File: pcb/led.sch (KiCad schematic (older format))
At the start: 15 parts, among them J1 CONN_01X04, J2 CONN_01X04, J3 CONN_01X01, J4 CONN_01X01, J5 CONN_01X01, J6 CONN_01X01, U1 DSN-MINI-360, U2 MAX485, U3 MAX485

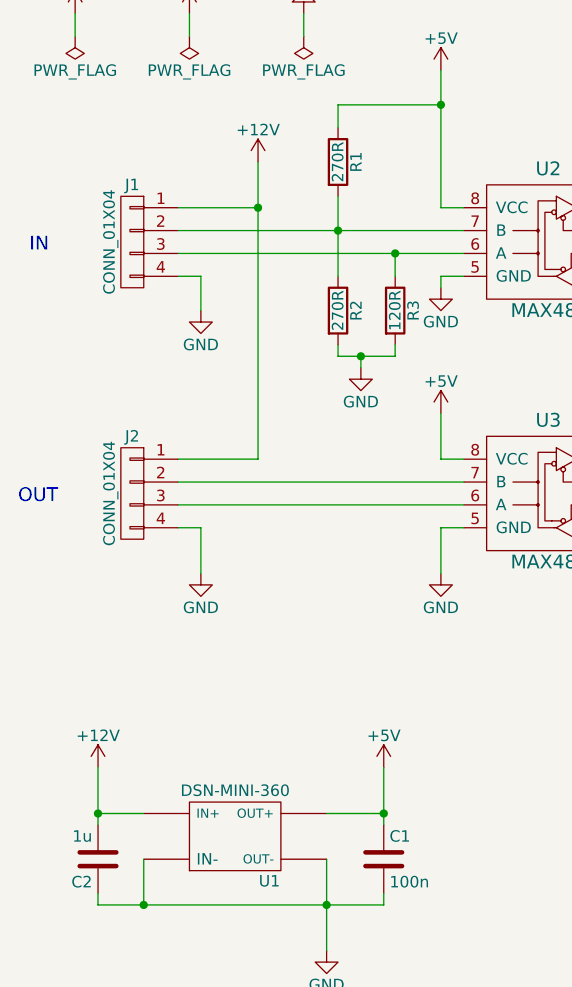
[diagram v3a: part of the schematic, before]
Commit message: Change to 3.5 mm pitch connectors. Finalize PCB layout.
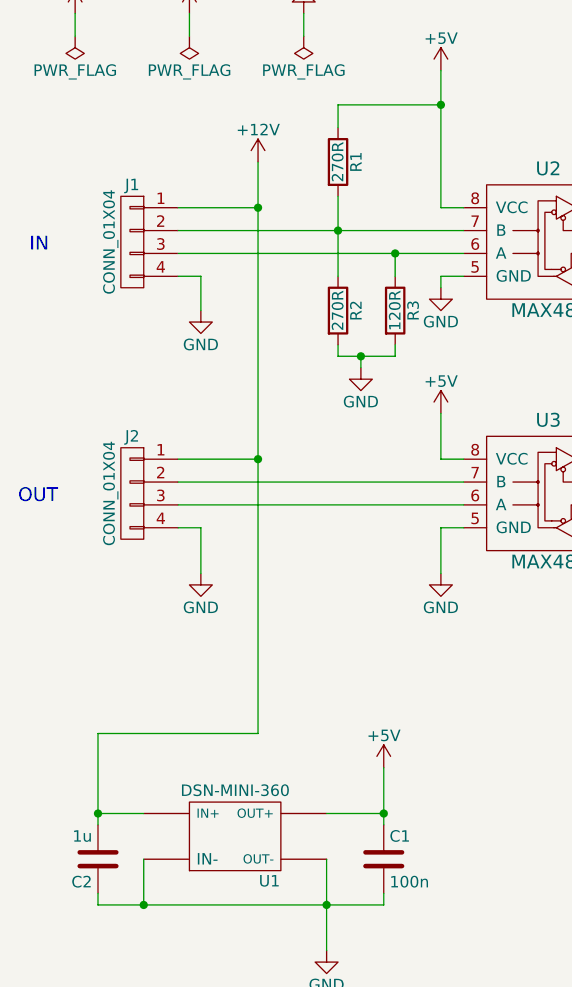
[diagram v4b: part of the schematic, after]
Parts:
- J1, J2: footprint Connectors_Phoenix:PhoenixContact_MSTBA-G_04x5.08mm_Angled -> Connectors_Phoenix:PhoenixContact_MC-G_04x3.50mm_Angled
- J3, J4, J5, J6: footprint Wire_Pads:SolderWirePad_single_1-5mmDrill -> Wire_Pads:SolderWirePad_single_1-2mmDrill
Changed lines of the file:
@@
 $EndDescr
 $Comp
-L +12V #PWR01
+L +12V #PWR5
 U 1 1 58CEE432
 P 1800 1550
-F 0 "#PWR01" H 1800 1400 50  0001 C CNN
+F 0 "#PWR5" H 1800 1400 50  0001 C CNN
 F 1 "+12V" H 1800 1690 50  0000 C CNN
 F 2 "" H 1800 1550 50  0001 C CNN
@@
 $EndComp
 $Comp
-L +12V #PWR02
+L +12V #PWR1
 U 1 1 58CEF552
 P 1000 900
-F 0 "#PWR02" H 1000 750 50  0001 C CNN
+F 0 "#PWR1" H 1000 750 50  0001 C CNN
 F 1 "+12V" H 1000 1040 50  0000 C CNN
 F 2 "" H 1000 900 50  0001 C CNN
@@
 Text Notes 800  1950 0    60   ~ 0
 IN
-Text Notes 5500 1900 0    60   ~ 0
-+5V
-Text Notes 5500 2150 0    60   ~ 0
-DI
-Text Notes 5500 2400 0    60   ~ 0
-DO
-Text Notes 5500 2650 0    60   ~ 0
-GND
 $Comp
 L C C2
@@
 $EndComp
 $Comp
-L PWR_FLAG #FLG03
+L PWR_FLAG #FLG1
 U 1 1 58CF1109
 P 1000 1000
-F 0 "#FLG03" H 1000 1075 50  0001 C CNN
+F 0 "#FLG1" H 1000 1075 50  0001 C CNN
 F 1 "PWR_FLAG" H 1000 1150 50  0000 C CNN
 F 2 "" H 1000 1000 50  0001 C CNN
@@
 $EndComp
 $Comp
-L +5V #PWR04
+L +5V #PWR16
 U 1 1 58CEF58A
 P 4950 1750
-F 0 "#PWR04" H 4950 1600 50  0001 C CNN
+F 0 "#PWR16" H 4950 1600 50  0001 C CNN
 F 1 "+5V" H 4950 1890 50  0000 C CNN
 F 2 "" H 4950 1750 50  0001 C CNN
@@
 $EndComp
 $Comp
-L GND #PWR05
+L GND #PWR17
 U 1 1 58CEF3EE
 P 4950 2700
-F 0 "#PWR05" H 4950 2450 50  0001 C CNN
+F 0 "#PWR17" H 4950 2450 50  0001 C CNN
 F 1 "GND" H 4950 2550 50  0000 C CNN
 F 2 "" H 4950 2700 50  0001 C CNN
@@
 F 0 "J1" H 1250 2150 50  0000 C CNN
 F 1 "CONN_01X04" V 1350 1900 50  0000 C CNN
-F 2 "Connectors_Phoenix:PhoenixContact_MSTBA-G_04x5.08mm_Angled" H 1250 1900 50  0001 C CNN
+F 2 "Connectors_Phoenix:PhoenixContact_MC-G_04x3.50mm_Angled" H 1250 1900 50  0001 C CNN
 F 3 "" H 1250 1900 50  0001 C CNN
 	1    1250 1900
@@
 F 0 "J2" H 1250 3250 50  0000 C CNN
 F 1 "CONN_01X04" V 1350 3000 50  0000 C CNN
-F 2 "Connectors_Phoenix:PhoenixContact_MSTBA-G_04x5.08mm_Angled" H 1250 3000 50  0001 C CNN
+F 2 "Connectors_Phoenix:PhoenixContact_MC-G_04x3.50mm_Angled" H 1250 3000 50  0001 C CNN
 F 3 "" H 1250 3000 50  0001 C CNN
 	1    1250 3000
@@
 $EndComp
 $Comp
-L GND #PWR06
+L GND #PWR3
 U 1 1 58D6FA50
 P 1550 2200
-F 0 "#PWR06" H 1550 1950 50  0001 C CNN
+F 0 "#PWR3" H 1550 1950 50  0001 C CNN
 F 1 "GND" H 1550 2050 50  0000 C CNN
 F 2 "" H 1550 2200 50  0001 C CNN
@@
 $EndComp
 $Comp
-L GND #PWR07
+L GND #PWR4
 U 1 1 58D6FA70
 P 1550 3350
-F 0 "#PWR07" H 1550 3100 50  0001 C CNN
+F 0 "#PWR4" H 1550 3100 50  0001 C CNN
 F 1 "GND" H 1550 3200 50  0000 C CNN
 F 2 "" H 1550 3350 50  0001 C CNN
@@
 OUT
 $Comp
-L GND #PWR08
+L GND #PWR7
 U 1 1 58D6FB2D
 P 2100 5000
-F 0 "#PWR08" H 2100 4750 50  0001 C CNN
+F 0 "#PWR7" H 2100 4750 50  0001 C CNN
 F 1 "GND" H 2100 4850 50  0000 C CNN
 F 2 "" H 2100 5000 50  0001 C CNN
@@
 	1000 900  1000 1000
 Wire Wire Line
-	1100 4200 1100 4450
+	1100 4050 1100 4450
 $Comp
 L MAX485 U3
@@
 	2700 3050 1450 3050
 $Comp
-L +5V #PWR09
+L +5V #PWR10
 U 1 1 58D7034E
 P 2600 1150
-F 0 "#PWR09" H 2600 1000 50  0001 C CNN
+F 0 "#PWR10" H 2600 1000 50  0001 C CNN
 F 1 "+5V" H 2600 1290 50  0000 C CNN
 F 2 "" H 2600 1150 50  0001 C CNN
@@
 $EndComp
 $Comp
-L +5V #PWR010
+L +5V #PWR12
 U 1 1 58D70372
 P 2600 2650
-F 0 "#PWR010" H 2600 2500 50  0001 C CNN
+F 0 "#PWR12" H 2600 2500 50  0001 C CNN
 F 1 "+5V" H 2600 2790 50  0000 C CNN
 F 2 "" H 2600 2650 50  0001 C CNN
@@
 	2600 1150 2600 1750
 $Comp
-L GND #PWR011
+L GND #PWR11
 U 1 1 58D703EC
 P 2600 2100
-F 0 "#PWR011" H 2600 1850 50  0001 C CNN
+F 0 "#PWR11" H 2600 1850 50  0001 C CNN
 F 1 "GND" H 2600 1950 50  0000 C CNN
 F 2 "" H 2600 2100 50  0001 C CNN
@@
 $EndComp
 $Comp
-L GND #PWR012
+L GND #PWR13
 U 1 1 58D70410
 P 2600 3350
-F 0 "#PWR012" H 2600 3100 50  0001 C CNN
+F 0 "#PWR13" H 2600 3100 50  0001 C CNN
 F 1 "GND" H 2600 3200 50  0000 C CNN
 F 2 "" H 2600 3350 50  0001 C CNN
@@
 	3900 3150 3500 3150
 $Comp
-L +5V #PWR013
+L +5V #PWR15
 U 1 1 58D70509
 P 3600 2650
-F 0 "#PWR013" H 3600 2500 50  0001 C CNN
+F 0 "#PWR15" H 3600 2500 50  0001 C CNN
 F 1 "+5V" H 3600 2790 50  0000 C CNN
 F 2 "" H 3600 2650 50  0001 C CNN
@@
 Connection ~ 3600 2950
 $Comp
-L GND #PWR014
+L GND #PWR14
 U 1 1 58D7059A
 P 3600 2100
-F 0 "#PWR014" H 3600 1850 50  0001 C CNN
+F 0 "#PWR14" H 3600 1850 50  0001 C CNN
 F 1 "GND" H 3600 1950 50  0000 C CNN
 F 2 "" H 3600 2100 50  0001 C CNN
@@
 $EndComp
 Wire Wire Line
-	1800 1550 1800 2850
+	1800 1550 1800 4050
 Wire Wire Line
 	1800 2850 1450 2850
@@
 $EndComp
 $Comp
-L GND #PWR015
+L GND #PWR8
 U 1 1 58D707AE
 P 2250 2450
-F 0 "#PWR015" H 2250 2200 50  0001 C CNN
+F 0 "#PWR8" H 2250 2200 50  0001 C CNN
 F 1 "GND" H 2250 2300 50  0000 C CNN
 F 2 "" H 2250 2450 50  0001 C CNN
@@
 Connection ~ 2400 1950
 $Comp
-L +5V #PWR016
+L +5V #PWR2
 U 1 1 58D70CC2
 P 1500 900
-F 0 "#PWR016" H 1500 750 50  0001 C CNN
+F 0 "#PWR2" H 1500 750 50  0001 C CNN
 F 1 "+5V" H 1500 1040 50  0000 C CNN
 F 2 "" H 1500 900 50  0001 C CNN
@@
 $EndComp
 $Comp
-L PWR_FLAG #FLG017
+L PWR_FLAG #FLG2
 U 1 1 58D70CEA
 P 1500 1000
-F 0 "#FLG017" H 1500 1075 50  0001 C CNN
+F 0 "#FLG2" H 1500 1075 50  0001 C CNN
 F 1 "PWR_FLAG" H 1500 1150 50  0000 C CNN
 F 2 "" H 1500 1000 50  0001 C CNN
@@
 	1500 1000 1500 900
 $Comp
-L PWR_FLAG #FLG018
+L PWR_FLAG #FLG3
 U 1 1 58D70D82
 P 2000 1000
-F 0 "#FLG018" H 2000 1075 50  0001 C CNN
+F 0 "#FLG3" H 2000 1075 50  0001 C CNN
 F 1 "PWR_FLAG" H 2000 1150 50  0000 C CNN
 F 2 "" H 2000 1000 50  0001 C CNN
@@
 $EndComp
 $Comp
-L GND #PWR019
+L GND #PWR6
 U 1 1 58D70DAA
 P 2000 900
-F 0 "#PWR019" H 2000 650 50  0001 C CNN
+F 0 "#PWR6" H 2000 650 50  0001 C CNN
 F 1 "GND" H 2000 750 50  0000 C CNN
 F 2 "" H 2000 900 50  0001 C CNN
@@
 F 0 "J3" H 5250 1950 50  0000 C CNN
 F 1 "CONN_01X01" V 5350 1850 50  0001 C CNN
-F 2 "Wire_Pads:SolderWirePad_single_1-5mmDrill" H 5250 1850 50  0001 C CNN
+F 2 "Wire_Pads:SolderWirePad_single_1-2mmDrill" H 5250 1850 50  0001 C CNN
 F 3 "" H 5250 1850 50  0001 C CNN
 	1    5250 1850
@@
 F 0 "J4" H 5250 2200 50  0000 C CNN
 F 1 "CONN_01X01" V 5350 2100 50  0001 C CNN
-F 2 "Wire_Pads:SolderWirePad_single_1-5mmDrill" H 5250 2100 50  0001 C CNN
+F 2 "Wire_Pads:SolderWirePad_single_1-2mmDrill" H 5250 2100 50  0001 C CNN
 F 3 "" H 5250 2100 50  0001 C CNN
 	1    5250 2100
@@
 F 0 "J5" H 5250 2450 50  0000 C CNN
 F 1 "CONN_01X01" V 5350 2350 50  0001 C CNN
-F 2 "Wire_Pads:SolderWirePad_single_1-5mmDrill" H 5250 2350 50  0001 C CNN
+F 2 "Wire_Pads:SolderWirePad_single_1-2mmDrill" H 5250 2350 50  0001 C CNN
 F 3 "" H 5250 2350 50  0001 C CNN
 	1    5250 2350
@@
 F 0 "J6" H 5250 2700 50  0000 C CNN
 F 1 "CONN_01X01" V 5350 2600 50  0001 C CNN
-F 2 "Wire_Pads:SolderWirePad_single_1-5mmDrill" H 5250 2600 50  0001 C CNN
+F 2 "Wire_Pads:SolderWirePad_single_1-2mmDrill" H 5250 2600 50  0001 C CNN
 F 3 "" H 5250 2600 50  0001 C CNN
 	1    5250 2600
@@
 Wire Wire Line
 	1450 1750 1800 1750
-$Comp
-L +12V #PWR020
-U 1 1 58E11721
-P 1100 4200
-F 0 "#PWR020" H 1100 4050 50  0001 C CNN
-F 1 "+12V" H 1100 4340 50  0000 C CNN
-F 2 "" H 1100 4200 50  0001 C CNN
-F 3 "" H 1100 4200 50  0001 C CNN
-	1    1100 4200
-	1    0    0    -1
-$EndComp
 Wire Wire Line
 	1100 4400 1300 4400
 $Comp
-L +5V #PWR021
+L +5V #PWR9
 U 1 1 58E11F02
 P 2350 4200
-F 0 "#PWR021" H 2350 4050 50  0001 C CNN
+F 0 "#PWR9" H 2350 4050 50  0001 C CNN
 F 1 "+5V" H 2350 4340 50  0000 C CNN
 F 2 "" H 2350 4200 50  0001 C CNN
@@
 	1    0    0    -1
 $EndComp
+Wire Wire Line
+	1800 4050 1100 4050
+Connection ~ 1800 2850
+Text Notes 5500 2650 0    60   ~ 0
+GND
+Text Notes 5500 2150 0    60   ~ 0
+DI
+Text Notes 5500 2400 0    60   ~ 0
+DO
+Text Notes 5500 1900 0    60   ~ 0
++5V
 $EndSCHEMATC
